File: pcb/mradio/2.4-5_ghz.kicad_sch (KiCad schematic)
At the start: 0 parts

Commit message: 2.4/5 GHz schematic
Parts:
- added C1, C2: 10uF, MDT420E01001:AMPHENOL_MDT420E01001, symbol Device:C
- added D1, D2: LED, symbol Device:LED
- added J2: MDT420E01001, MDT420E01001:AMPHENOL_MDT420E01001, symbol symbols:MDT420E01001
- added R1, R2: R, symbol Device:R
- added XTAL1: SIT1533AI-H4-DCC-32.768E, XTAL4_SiT1533_SIT, symbol symbols:SIT1533AI-H4-DCC-32.768E
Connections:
- new net: D1.2 (A), R1.2
- new net: D2.2 (A), R2.2
- new net: D2.1 (K), J2.16
- new net: J2.50, XTAL1.3 (CLK_Out)
- new net: D1.1 (K), J2.6
- new net +3.3V: C1.1, C2.1, J2.2, J2.4, J2.72, J2.74, R1.1, R2.1, XTAL1.4 (Vdd)
- new net GND: C1.2, C2.2, J2.1, J2.18, J2.33, J2.39, J2.45, J2.51, J2.54, J2.57, J2.63, J2.69, J2.7, J2.75, XTAL1.2 (GND)
- new net IF573_SDIO_CLK: J2.9
- new net IF573_SDIO_CMD: J2.11
- new net IF573_SDIO_D0: J2.13
- new net IF573_SDIO_D1: J2.15
- new net IF573_SDIO_D2: J2.17
- new net IF573_SDIO_D3: J2.19
- new net WL_DEV_WAKE: J2.40
- new net WL_HOST_WAKE: J2.21
- new net WL_REG_ON: J2.56
- no-connect marks 0 -> 40

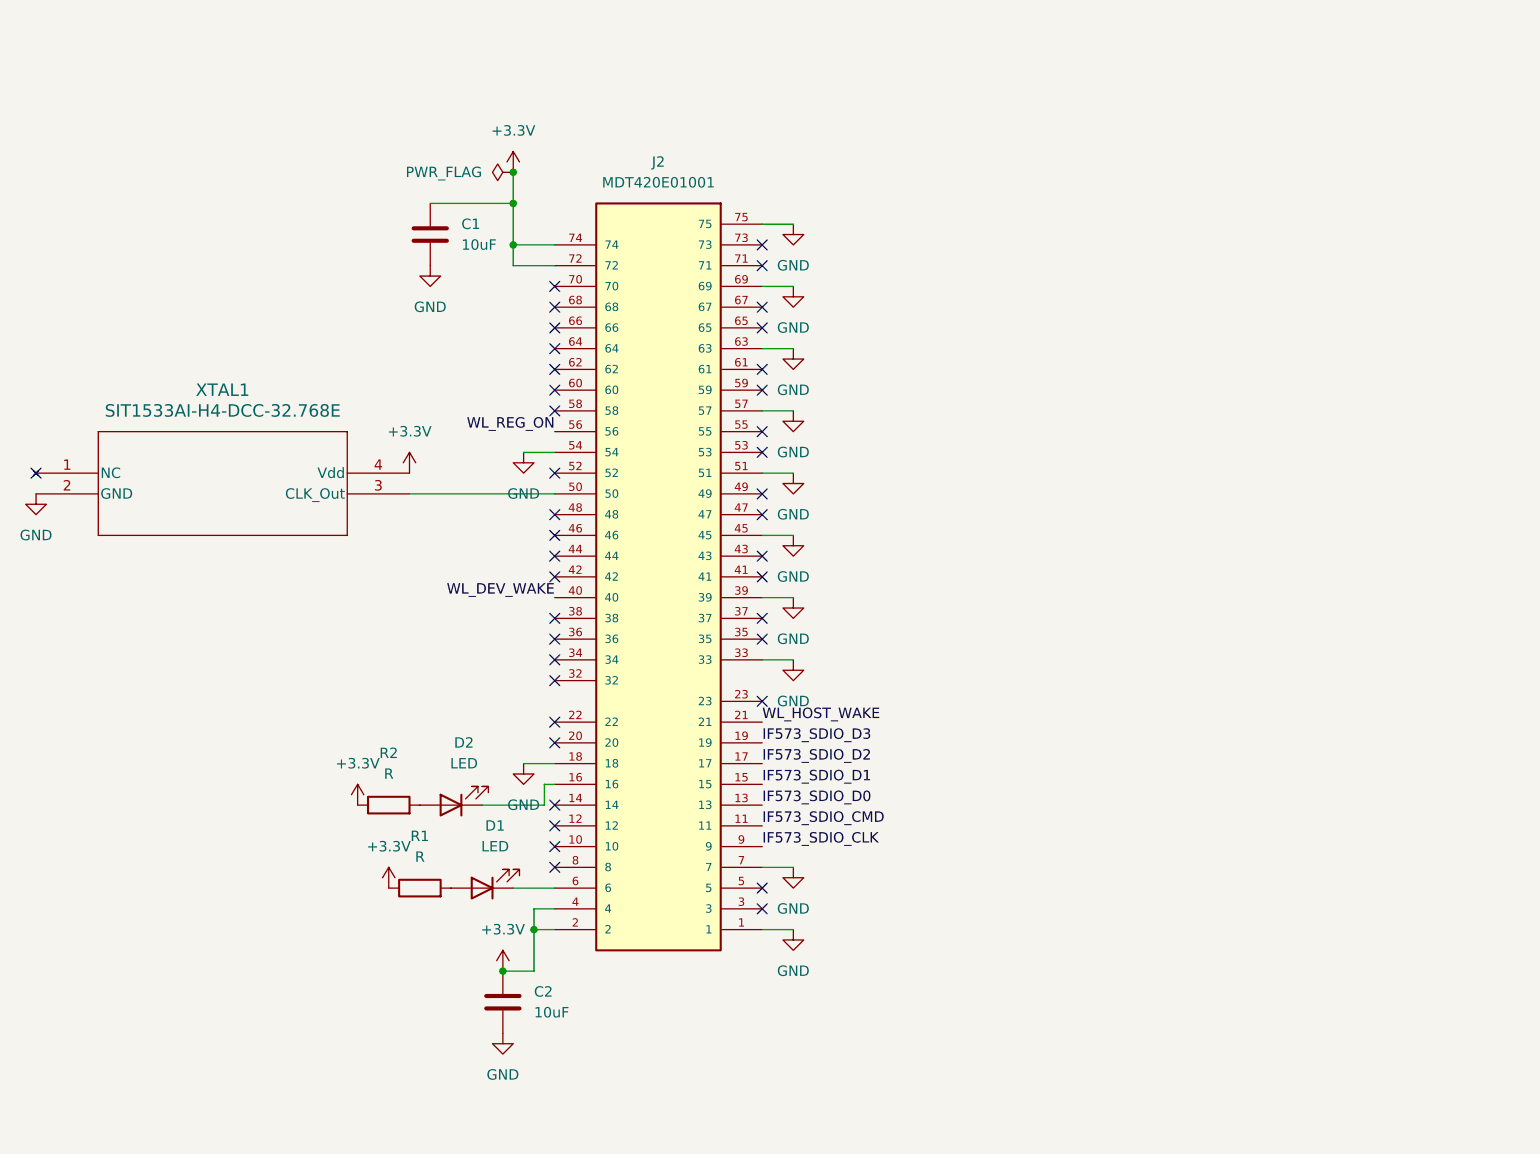
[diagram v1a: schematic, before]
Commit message: Add level shifters to 2.4/5 GHz
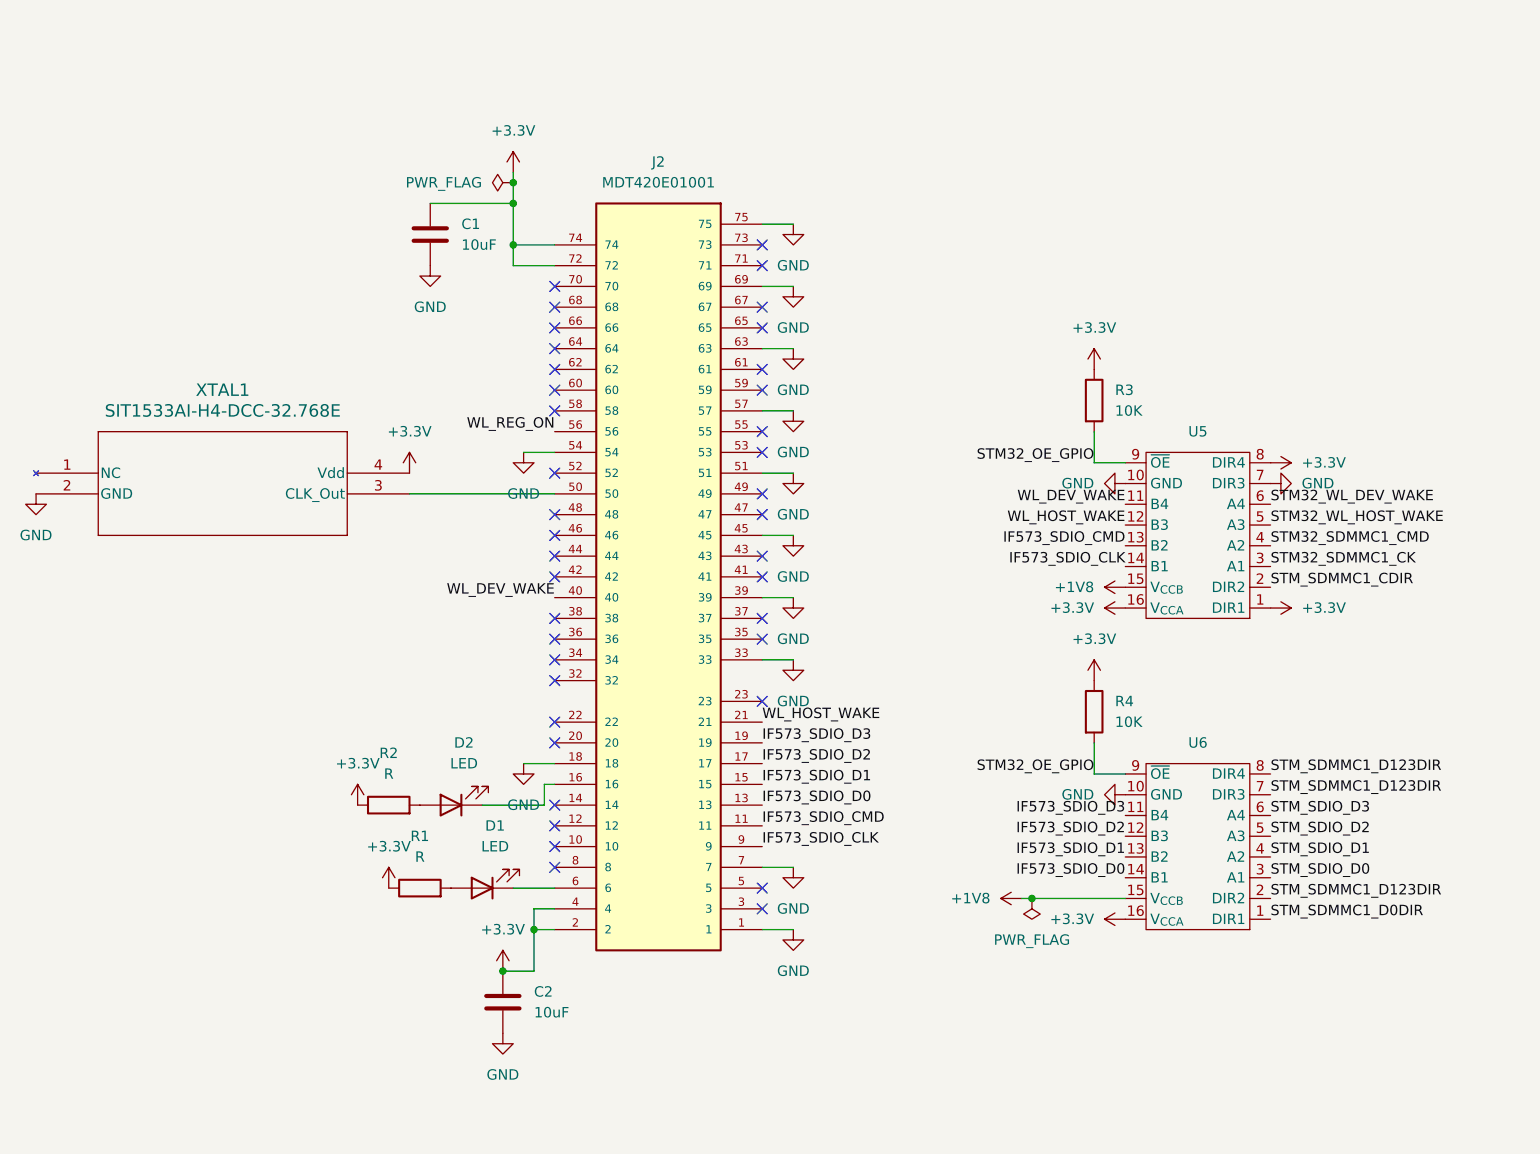
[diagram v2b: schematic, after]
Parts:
- added R3, R4: 10K, symbol Device:R
- added U5, U6: (no value), Package_SO:TSSOP-16_4.4x5mm_P0.65mm, symbol 74AVC4T774QPWRQ1:74AVC4T774QPWRQ1
- XTAL1: footprint XTAL4_SiT1533_SIT -> SiT1533:XTAL4_SiT1533_SIT
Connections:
- net +3.3V: now also R3.1, R4.1, U5.1 (DIR1), U5.16 (V_{CCA}), U5.8 (DIR4), U6.16 (V_{CCA})
- net GND: now also U5.10 (GND), U5.7 (DIR3), U6.10 (GND)
- net IF573_SDIO_CLK: now also U5.14 (B1)
- net IF573_SDIO_CMD: now also U5.13 (B2)
- net IF573_SDIO_D0: now also U6.14 (B1)
- net IF573_SDIO_D1: now also U6.13 (B2)
- net IF573_SDIO_D2: now also U6.12 (B3)
- net IF573_SDIO_D3: now also U6.11 (B4)
- net WL_DEV_WAKE: now also U5.11 (B4)
- net WL_HOST_WAKE: now also U5.12 (B3)
- new net +1V8: U5.15 (V_{CCB}), U6.15 (V_{CCB})
- new net STM32_OE_GPIO: R3.2, R4.2, U5.9 (~{OE}), U6.9 (~{OE})
- new net STM32_SDMMC1_CK: U5.3 (A1)
- new net STM32_SDMMC1_CMD: U5.4 (A2)
- new net STM32_WL_DEV_WAKE: U5.6 (A4)
- new net STM32_WL_HOST_WAKE: U5.5 (A3)
- new net STM_SDIO_D0: U6.3 (A1)
- new net STM_SDIO_D1: U6.4 (A2)
- new net STM_SDIO_D2: U6.5 (A3)
- new net STM_SDIO_D3: U6.6 (A4)
- new net STM_SDMMC1_CDIR: U5.2 (DIR2)
- new net STM_SDMMC1_D0DIR: U6.1 (DIR1)
- new net STM_SDMMC1_D123DIR: U6.2 (DIR2), U6.7 (DIR3), U6.8 (DIR4)
- no-connect marks 40 -> 39

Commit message: Add some capacitor jits
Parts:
- added C11, C12, C13, C14: 0.1uF, symbol Device:C
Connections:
- net +1V8: now also C12.1, C14.1
- net +3.3V: now also C11.1, C13.1
- net GND: now also C11.2, C12.2, C13.2, C14.2
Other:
- moved on the sheet: R4, U6

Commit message: Add pull ups to WiFi, change annotation method
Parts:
- added R501, R502, R503, R504, R505: 10K, symbol Device:R
- R508: renamed from R2; value R -> 1K
- R509: renamed from R1; value R -> 1K
- renumbered C1 to C501, C14 to C502, C13 to C503, C2 to C504, C12 to C505, C11 to C506, D2 to D501, D1 to D502, J2 to J501, R3 to R506, R4 to R507, U5 to U501, U6 to U502, XTAL1 to XTAL501
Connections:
- net +3.3V: now also R501.1, R502.1, R503.1, R504.1, R505.1
- net IF573_SDIO_CMD: now also R505.2
- net IF573_SDIO_D0: now also R501.2
- net IF573_SDIO_D1: now also R502.2
- net IF573_SDIO_D2: now also R503.2
- net IF573_SDIO_D3: now also R504.2
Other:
- moved on the sheet: C502, C503, C505, C506, R506, R507, U501, U502

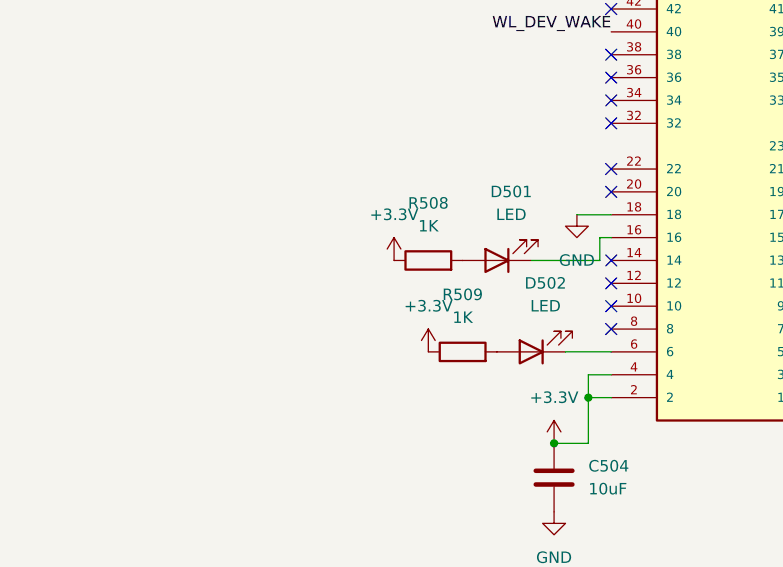
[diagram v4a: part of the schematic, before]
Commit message: Add footprints
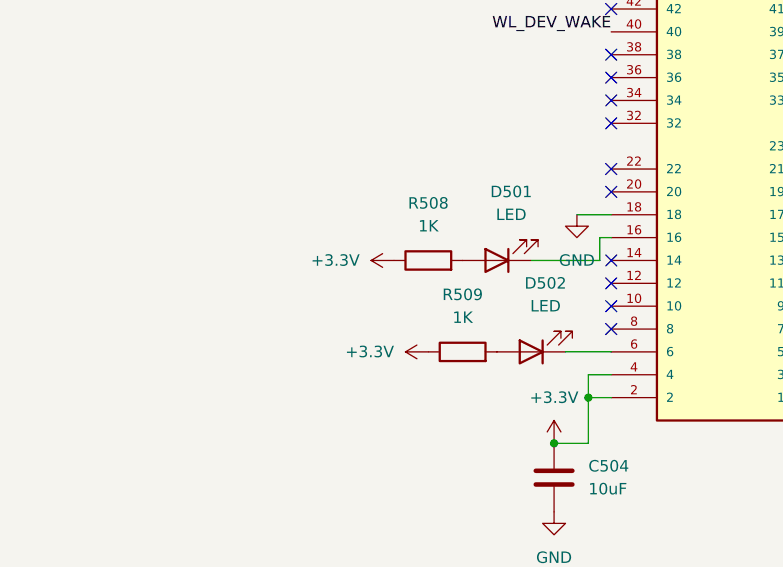
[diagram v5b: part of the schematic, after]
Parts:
- C501, C504: footprint MDT420E01001:AMPHENOL_MDT420E01001 -> Capacitor_SMD:C_0603_1608Metric
- C502, C503, C505, C506: footprint (none) -> Capacitor_SMD:C_0603_1608Metric
- R501, R502, R503, R504, R505, R506, R507, R508, R509: footprint (none) -> Resistor_SMD:R_0603_1608Metric
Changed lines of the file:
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@@
 			)
 		)
-		(property "Footprint" ""
+		(property "Footprint" "Resistor_SMD:R_0603_1608Metric"
 			(at 104.14 131.318 90)
 			(hide yes)
@@
 			)
 		)
-		(property "Footprint" ""
+		(property "Footprint" "Resistor_SMD:R_0603_1608Metric"
 			(at 196.342 33.02 90)
 			(hide yes)
@@
 			)
 		)
-		(property "Footprint" "MDT420E01001:AMPHENOL_MDT420E01001"
+		(property "Footprint" "Capacitor_SMD:C_0603_1608Metric"
 			(at 115.2652 147.32 0)
 			(hide yes)
@@
 	(symbol
 		(lib_id "power:+3.3V")
-		(at 100.33 129.54 0)
+		(at 100.33 129.54 90)
 		(unit 1)
 		(body_style 1)
@@
 		(fields_autoplaced yes)
 		(property "Reference" "#PWR0528"
-			(at 100.33 133.35 0)
+			(at 104.14 129.54 0)
 			(hide yes)
 			(show_name no)
@@
 		)
 		(property "Value" "+3.3V"
-			(at 100.33 124.46 0)
+			(at 96.52 129.5399 90)
 			(show_name no)
 			(do_not_autoplace no)
@@
 					(size 1.27 1.27)
 				)
+				(justify left)
 			)
 		)
@@
 	(symbol
 		(lib_id "power:+3.3V")
-		(at 96.52 119.38 0)
+		(at 96.52 119.38 90)
 		(unit 1)
 		(body_style 1)
@@
 		(fields_autoplaced yes)
 		(property "Reference" "#PWR0526"
-			(at 96.52 123.19 0)
+			(at 100.33 119.38 0)
 			(hide yes)
 			(show_name no)
@@
 		)
 		(property "Value" "+3.3V"
-			(at 96.52 114.3 0)
+			(at 92.71 119.3799 90)
 			(show_name no)
 			(do_not_autoplace no)
@@
 					(size 1.27 1.27)
 				)
+				(justify left)
 			)
 		)
@@
 			)
 		)
-		(property "Footprint" ""
+		(property "Footprint" "Capacitor_SMD:C_0603_1608Metric"
 			(at 177.4952 97.79 0)
 			(hide yes)
@@
 			)
 		)
-		(property "Footprint" ""
+		(property "Footprint" "Resistor_SMD:R_0603_1608Metric"
 			(at 100.33 121.158 90)
 			(hide yes)
@@
 			)
 		)
-		(property "Footprint" ""
+		(property "Footprint" "Resistor_SMD:R_0603_1608Metric"
 			(at 191.262 120.65 90)
 			(hide yes)
@@
 			)
 		)
-		(property "Footprint" ""
+		(property "Footprint" "Resistor_SMD:R_0603_1608Metric"
 			(at 169.672 33.02 90)
 			(hide yes)
@@
 			)
 		)
-		(property "Footprint" ""
+		(property "Footprint" "Resistor_SMD:R_0603_1608Metric"
 			(at 187.452 67.31 90)
 			(hide yes)
@@
 			)
 		)
-		(property "Footprint" ""
+		(property "Footprint" "Resistor_SMD:R_0603_1608Metric"
 			(at 178.562 33.02 90)
 			(hide yes)
@@
 			)
 		)
-		(property "Footprint" ""
+		(property "Footprint" "Capacitor_SMD:C_0603_1608Metric"
 			(at 180.0352 151.13 0)
 			(hide yes)
@@
 			)
 		)
-		(property "Footprint" "MDT420E01001:AMPHENOL_MDT420E01001"
+		(property "Footprint" "Capacitor_SMD:C_0603_1608Metric"
 			(at 106.3752 53.34 0)
 			(hide yes)
@@
 			)
 		)
-		(property "Footprint" ""
+		(property "Footprint" "Resistor_SMD:R_0603_1608Metric"
 			(at 187.452 33.02 90)
 			(hide yes)
@@
 			)
 		)
-		(property "Footprint" ""
+		(property "Footprint" "Resistor_SMD:R_0603_1608Metric"
 			(at 205.232 33.02 90)
 			(hide yes)
@@
 			)
 		)
-		(property "Footprint" ""
+		(property "Footprint" "Capacitor_SMD:C_0603_1608Metric"
 			(at 192.7352 100.33 0)
 			(hide yes)
@@
 			)
 		)
-		(property "Footprint" ""
+		(property "Footprint" "Capacitor_SMD:C_0603_1608Metric"
 			(at 196.5452 153.67 0)
 			(hide yes)
